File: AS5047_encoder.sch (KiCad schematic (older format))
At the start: 4 parts, among them P1 CONN_01X07, U1 AS5047

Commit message: Change connector and update component associations.
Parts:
- C1, C2: footprint (none) -> Capacitors_SMD:C_0603
- P1: footprint (none) -> w_conn_jst-ph:s7b-ph-kl
- U1: footprint (none) -> Housings_SSOP:TSSOP-14_4.4x5mm_Pitch0.65mm
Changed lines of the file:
@@
 F 0 "U1" H 5350 4050 60  0000 C TNN
 F 1 "AS5047" H 5400 3150 60  0000 C BNN
-F 2 "" H 5400 3150 60  0001 C CNN
+F 2 "Housings_SSOP:TSSOP-14_4.4x5mm_Pitch0.65mm" H 5400 3150 60  0001 C CNN
 F 3 "" H 5400 3150 60  0001 C CNN
 	1    5400 3600
@@
 F 0 "C1" H 6225 3850 50  0000 L CNN
 F 1 "C" H 6225 3650 50  0000 L CNN
-F 2 "" H 6238 3600 50  0001 C CNN
+F 2 "Capacitors_SMD:C_0603" H 6238 3600 50  0001 C CNN
 F 3 "" H 6200 3750 50  0001 C CNN
 	1    6200 3750
@@
 F 0 "C2" H 6525 3850 50  0000 L CNN
 F 1 "C" H 6525 3650 50  0000 L CNN
-F 2 "" H 6538 3600 50  0001 C CNN
+F 2 "Capacitors_SMD:C_0603" H 6538 3600 50  0001 C CNN
 F 3 "" H 6500 3750 50  0001 C CNN
 	1    6500 3750
@@
 $EndComp
 $Comp
-L GND #PWR2
+L GND #PWR01
 U 1 1 5A4901E0
 P 6850 4150
-F 0 "#PWR2" H 6850 3900 50  0001 C CNN
+F 0 "#PWR01" H 6850 3900 50  0001 C CNN
 F 1 "GND" H 6850 4000 50  0000 C CNN
 F 2 "" H 6850 4150 50  0001 C CNN
@@
 F 0 "P1" H 4150 4050 50  0000 C CNN
 F 1 "CONN_01X07" V 4250 3650 50  0000 C CNN
-F 2 "" H 4150 3650 50  0000 C CNN
+F 2 "w_conn_jst-ph:s7b-ph-kl" H 4150 3650 50  0001 C CNN
 F 3 "" H 4150 3650 50  0000 C CNN
 	1    4150 3650
@@
 Connection ~ 6050 3600
 $Comp
-L GND #PWR1
+L GND #PWR02
 U 1 1 5A49238E
 P 4800 3950
-F 0 "#PWR1" H 4800 3700 50  0001 C CNN
+F 0 "#PWR02" H 4800 3700 50  0001 C CNN
 F 1 "GND" H 4800 3800 50  0000 C CNN
 F 2 "" H 4800 3950 50  0001 C CNN

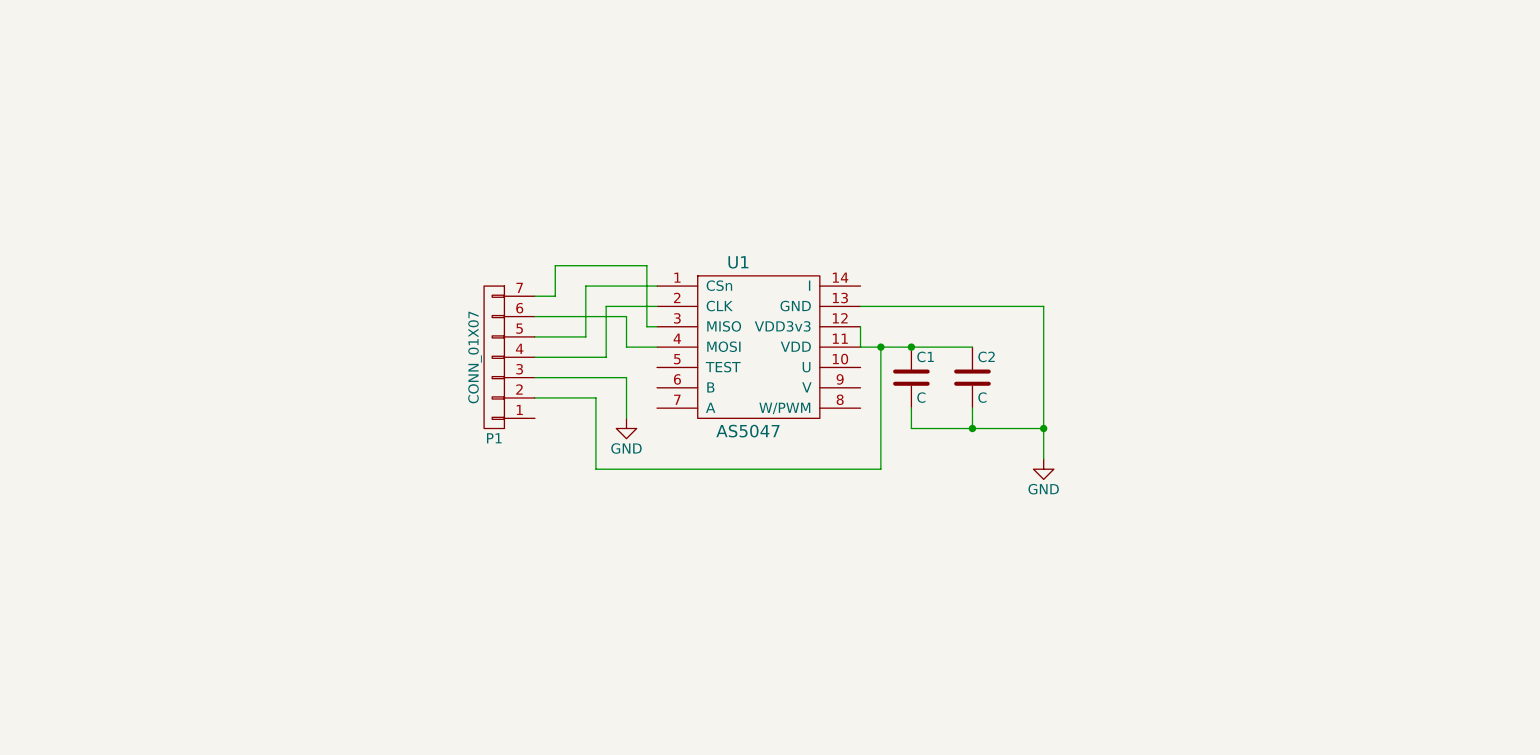
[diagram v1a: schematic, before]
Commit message: Fixed outline. Generated gerbers. Added BOM. Ordered a batch of boards.
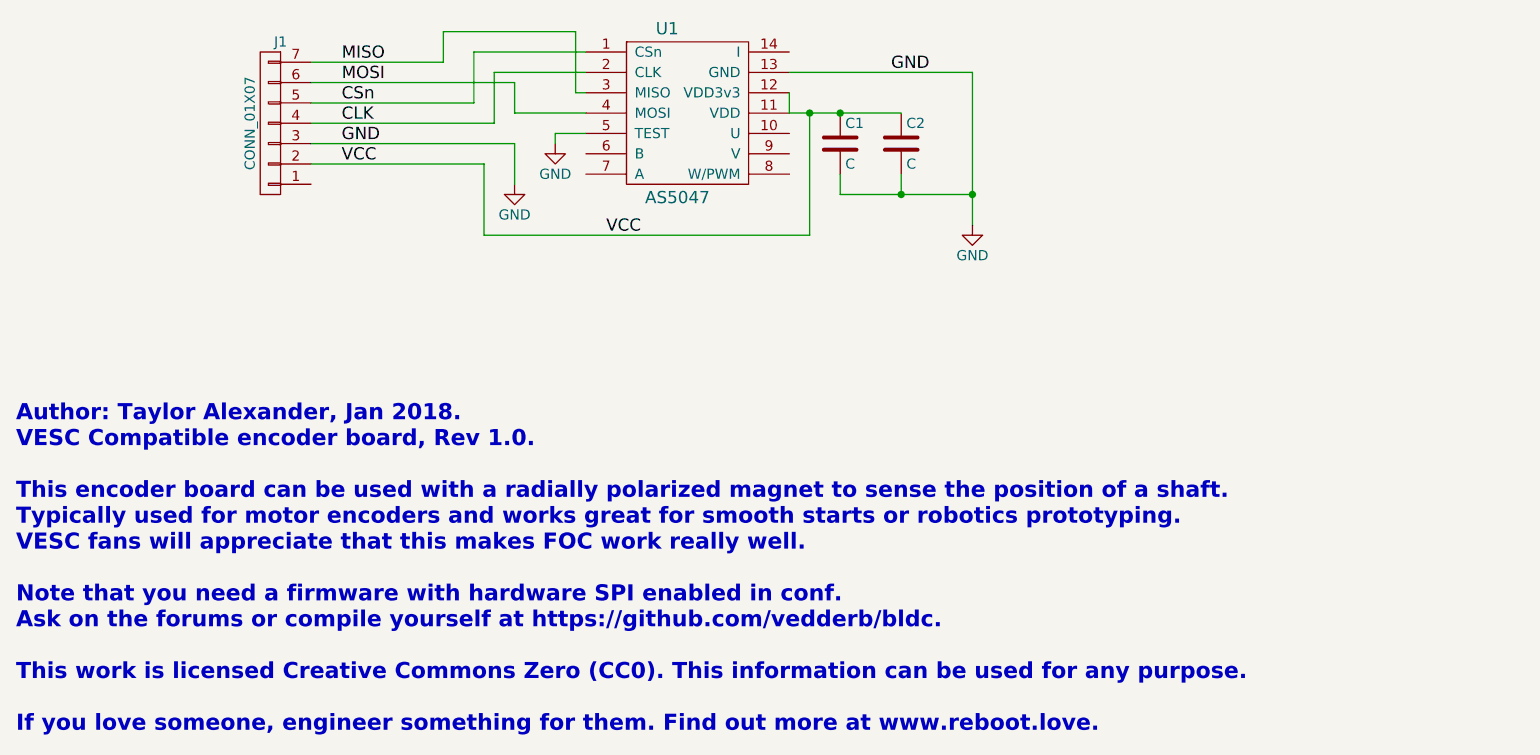
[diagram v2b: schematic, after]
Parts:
- renumbered P1 to J1
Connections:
- net GND: now also U1.5 (TEST)
- net CSn: now reaches J1.5 (P5), U1.1 (CSn)
- net VCC: now reaches C1.1, C2.1, J1.2 (P2), U1.11 (VDD), U1.12 (VDD3v3)
- net CLK: now reaches J1.4 (P4), U1.2 (CLK)
- net MISO: now reaches J1.7 (P7), U1.3 (MISO)
- net MOSI: now reaches J1.6 (P6), U1.4 (MOSI)
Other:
- note added: "Author: Taylor Alexander, Jan 2018.\nVESC Compatible encoder board, Rev 1.0.\n\nThis encoder board can be used with a radially polarized magnet to sense the position of a shaft.\nTypically used for motor encoders and works great for smooth starts or robotics prototyping.\nVESC fans will appreciate that this makes FOC work really well.\n\nNote that you need a firmware with hardware SPI enabled in 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"
- moved on the sheet: C1, C2, J1, U1
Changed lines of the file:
@@
 L AS5047 U1
 U 1 1 5A489C6C
-P 5400 3600
-F 0 "U1" H 5350 4050 60  0000 C TNN
-F 1 "AS5047" H 5400 3150 60  0000 C BNN
-F 2 "Housings_SSOP:TSSOP-14_4.4x5mm_Pitch0.65mm" H 5400 3150 60  0001 C CNN
-F 3 "" H 5400 3150 60  0001 C CNN
-	1    5400 3600
+P 5050 2450
+F 0 "U1" H 5000 2900 60  0000 C TNN
+F 1 "AS5047" H 5050 2000 60  0000 C BNN
+F 2 "Housings_SSOP:TSSOP-14_4.4x5mm_Pitch0.65mm" H 5050 2000 60  0001 C CNN
+F 3 "" H 5050 2000 60  0001 C CNN
+	1    5050 2450
 	1    0    0    -1
 $EndComp
@@
 L C C1
 U 1 1 5A4900D1
-P 6200 3750
-F 0 "C1" H 6225 3850 50  0000 L CNN
-F 1 "C" H 6225 3650 50  0000 L CNN
-F 2 "Capacitors_SMD:C_0603" H 6238 3600 50  0001 C CNN
-F 3 "" H 6200 3750 50  0001 C CNN
-	1    6200 3750
+P 5850 2600
+F 0 "C1" H 5875 2700 50  0000 L CNN
+F 1 "C" H 5875 2500 50  0000 L CNN
+F 2 "Capacitors_SMD:C_0603" H 5888 2450 50  0001 C CNN
+F 3 "" H 5850 2600 50  0001 C CNN
+	1    5850 2600
 	1    0    0    -1
 $EndComp
@@
 L C C2
 U 1 1 5A490198
-P 6500 3750
-F 0 "C2" H 6525 3850 50  0000 L CNN
-F 1 "C" H 6525 3650 50  0000 L CNN
-F 2 "Capacitors_SMD:C_0603" H 6538 3600 50  0001 C CNN
-F 3 "" H 6500 3750 50  0001 C CNN
-	1    6500 3750
+P 6150 2600
+F 0 "C2" H 6175 2700 50  0000 L CNN
+F 1 "C" H 6175 2500 50  0000 L CNN
+F 2 "Capacitors_SMD:C_0603" H 6188 2450 50  0001 C CNN
+F 3 "" H 6150 2600 50  0001 C CNN
+	1    6150 2600
 	1    0    0    -1
 $EndComp
@@
 L GND #PWR01
 U 1 1 5A4901E0
-P 6850 4150
-F 0 "#PWR01" H 6850 3900 50  0001 C CNN
-F 1 "GND" H 6850 4000 50  0000 C CNN
-F 2 "" H 6850 4150 50  0001 C CNN
-F 3 "" H 6850 4150 50  0001 C CNN
-	1    6850 4150
+P 6500 3000
+F 0 "#PWR01" H 6500 2750 50  0001 C CNN
+F 1 "GND" H 6500 2850 50  0000 C CNN
+F 2 "" H 6500 3000 50  0001 C CNN
+F 3 "" H 6500 3000 50  0001 C CNN
+	1    6500 3000
 	1    0    0    -1
 $EndComp
 Wire Wire Line
-	5950 3500 5950 3600
+	5600 2350 5600 2450
 $Comp
-L CONN_01X07 P1
+L CONN_01X07 J1
 U 1 1 5A49201F
-P 4150 3650
-F 0 "P1" H 4150 4050 50  0000 C CNN
-F 1 "CONN_01X07" V 4250 3650 50  0000 C CNN
-F 2 "w_conn_jst-ph:s7b-ph-kl" H 4150 3650 50  0001 C CNN
-F 3 "" H 4150 3650 50  0000 C CNN
-	1    4150 3650
+P 3050 2500
+F 0 "J1" H 3000 2100 50  0000 C CNN
+F 1 "CONN_01X07" V 3150 2500 50  0000 C CNN
+F 2 "w_conn_jst-ph:s7b-ph-kl" H 3050 2500 50  0001 C CNN
+F 3 "" H 3050 2500 50  0000 C CNN
+	1    3050 2500
 	-1   0    0    1
 $EndComp
 Wire Wire Line
-	5950 3600 6500 3600
-Connection ~ 6200 3600
+	5600 2450 6150 2450
+Connection ~ 5850 2450
 Wire Wire Line
-	6200 3900 6200 4000
+	5850 2750 5850 2850
 Wire Wire Line
-	6200 4000 6850 4000
+	5850 2850 6500 2850
 Wire Wire Line
-	6500 4000 6500 3900
+	6150 2850 6150 2750
 Wire Wire Line
-	6850 3400 6850 4150
-Connection ~ 6500 4000
+	6500 2250 6500 3000
+Connection ~ 6150 2850
 Wire Wire Line
-	5950 3400 6850 3400
-Connection ~ 6850 4000
+	5600 2250 6500 2250
+Connection ~ 6500 2850
 Wire Wire Line
-	4350 3850 4650 3850
+	3250 2700 4100 2700
 Wire Wire Line
-	4650 3850 4650 4200
+	4100 2700 4100 3050
 Wire Wire Line
-	4650 4200 6050 4200
+	4100 3050 5700 3050
 Wire Wire Line
-	6050 4200 6050 3600
-Connection ~ 6050 3600
+	5700 3050 5700 2450
+Connection ~ 5700 2450
 $Comp
 L GND #PWR02
 U 1 1 5A49238E
-P 4800 3950
-F 0 "#PWR02" H 4800 3700 50  0001 C CNN
-F 1 "GND" H 4800 3800 50  0000 C CNN
-F 2 "" H 4800 3950 50  0001 C CNN
-F 3 "" H 4800 3950 50  0001 C CNN
-	1    4800 3950
+P 4250 2800
+F 0 "#PWR02" H 4250 2550 50  0001 C CNN
+F 1 "GND" H 4250 2650 50  0000 C CNN
+F 2 "" H 4250 2800 50  0001 C CNN
+F 3 "" H 4250 2800 50  0001 C CNN
+	1    4250 2800
 	1    0    0    -1
 $EndComp
 Wire Wire Line
-	4350 3750 4800 3750
+	3250 2600 4250 2600
 Wire Wire Line
-	4800 3750 4800 3950
+	4250 2600 4250 2800
 Wire Wire Line
-	4350 3650 4700 3650
+	3250 2500 4150 2500
 Wire Wire Line
-	4700 3650 4700 3400
+	4150 2500 4150 2250
 Wire Wire Line
-	4700 3400 4950 3400
+	4150 2250 4600 2250
 Wire Wire Line
-	4350 3550 4600 3550
+	3250 2400 4050 2400
 Wire Wire Line
-	4600 3550 4600 3300
+	4050 2400 4050 2150
 Wire Wire Line
-	4600 3300 4950 3300
+	4050 2150 4600 2150
 Wire Wire Line
-	4350 3450 4800 3450
+	3250 2300 4250 2300
 Wire Wire Line
-	4800 3450 4800 3600
+	4250 2300 4250 2450
 Wire Wire Line
-	4800 3600 4950 3600
+	4250 2450 4600 2450
 Wire Wire Line
-	4350 3350 4450 3350
+	3250 2200 3900 2200
 Wire Wire Line
-	4450 3350 4450 3200
+	3900 2200 3900 2050
 Wire Wire Line
-	4450 3200 4900 3200
+	3900 2050 4550 2050
 Wire Wire Line
-	4900 3200 4900 3500
+	4550 2050 4550 2350
 Wire Wire Line
-	4900 3500 4950 3500
+	4550 2350 4600 2350
+Text Label 6100 2250 0    60   ~ 0
+GND
+Text Label 4700 3050 0    60   ~ 0
+VCC
+Text Label 3400 2200 0    60   ~ 0
+MISO
+Text Label 3400 2300 0    60   ~ 0
+MOSI
+Text Label 3400 2400 0    60   ~ 0
+CSn
+Text Label 3400 2500 0    60   ~ 0
+CLK
+Text Label 3400 2600 0    60   ~ 0
+GND
+Text Label 3400 2700 0    60   ~ 0
+VCC
+Text Notes 1800 5500 0    79   ~ 16
+Author: Taylor Alexander, Jan 2018.\nVESC Compatible encoder board, Rev 1.0.\n\nThis encoder board can be used with a radially polarized magnet to sense the position of a shaft.\nTypically used for motor encoders and works great for smooth starts or robotics prototyping.\nVESC fans will appreciate that this makes FOC work really well.\n\nNote that you need a firmware with hardware SPI enabled in conf.\nAsk on the forums or compile yourself at https://github.com/vedderb/bldc.\n\nThis work is licensed Creative Commons Zero (CC0). This information can be used for any purpose.\n\nIf you love someone, engineer something for them. Find out more at www.reboot.love.
+$Comp
+L GND #PWR03
+U 1 1 5A5EFC26
+P 4450 2600
+F 0 "#PWR03" H 4450 2350 50  0001 C CNN
+F 1 "GND" H 4450 2450 50  0000 C CNN
+F 2 "" H 4450 2600 50  0001 C CNN
+F 3 "" H 4450 2600 50  0001 C CNN
+	1    4450 2600
+	1    0    0    -1
+$EndComp
+Wire Wire Line
+	4600 2550 4450 2550
+Wire Wire Line
+	4450 2550 4450 2600
 $EndSCHEMATC
